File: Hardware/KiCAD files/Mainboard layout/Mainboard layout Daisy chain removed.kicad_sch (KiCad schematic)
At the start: 90 parts, among them J10 Conn_01x02, J11 Conn_01x04, J12 JST_06, J13 Conn_01x08, J14 Conn_01x08, J15 Screw_Terminal_2_P5.00mm, J17 PINHD_1x8_Male, J18 PINHD_1x8_Male, J19 PINHD_1x8_Male, J2 Screw_Terminal_2_P5.00mm, J20 PINHD_1x8_Male, J22 PINHD_1x8_Male, J23 PINHD_1x8_Male, J24 PINHD_1x8_Male, J25 Conn_01x04, J26 Conn_01x04, J27 Conn_01x04, J28 PINHD_1x8_Male, J3 Screw_Terminal_2_P3.50mm, J30 USB-A1VSB6, J31 JST_03, J32 USB-A1VSB6, J34 JST_03, J35 JST_03, J36 JST_03, J37 JST_03, J38 JST_03, J4 JST_06, J5 Conn_01x04, J6 JST_06, J7 JST_06, J8 Conn_01x06, J9 Conn_01x10, Q1 BS170, Q2 2DD1664, SW1 210-4MS, SW2 210-4MS, SW3 210-4MS, SW4 210-4MS, SW8 Push_Button, SW9 Push_Button, U1 CP2102-GM, U12 ESP32-S3-WROOM-1, U2 PCA9534PW_118, U4 PCA9534PW_118

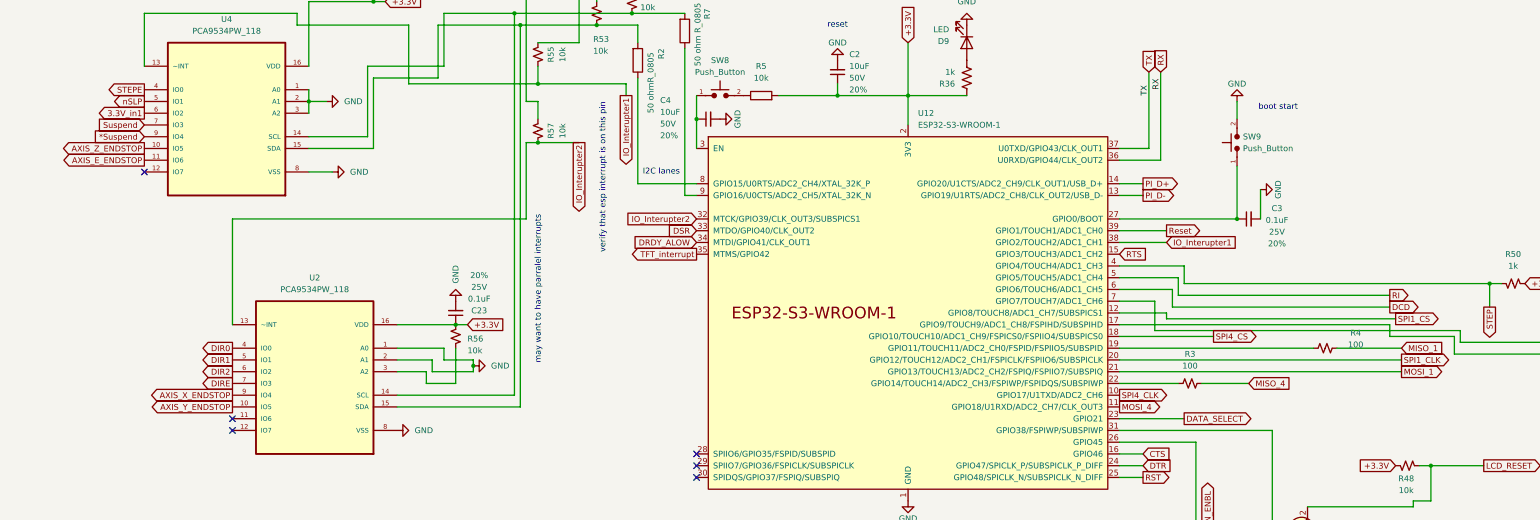
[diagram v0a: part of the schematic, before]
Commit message: part of the way through next iteration
Non-daisy chain Mainboard is ~50% through
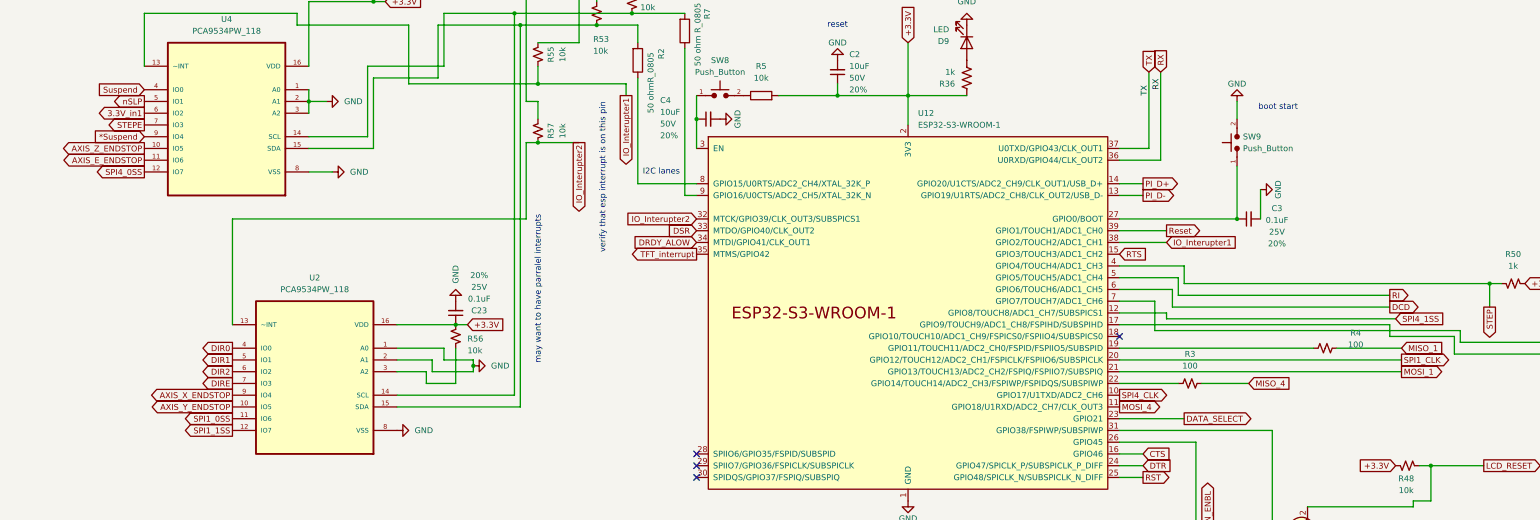
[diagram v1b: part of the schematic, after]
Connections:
- net SPI1_CS: no longer U12.12 (GPIO8/TOUCH8/ADC1_CH7/SUBSPICS1)
- net SPI4_CS: no longer U12.18 (GPIO10/TOUCH10/ADC1_CH9/FSPICS0/FSPIIO4/SUBSPICS0)
- net STEPE: now also U4.7 (IO3); no longer U4.4 (IO0)
- net Suspend: now also U4.4 (IO0); no longer U4.7 (IO3)
- net SPI4_0SS: now reaches U4.12 (IO7)
- net SPI1_0SS: now reaches U2.11 (IO6)
- net SPI1_1SS: now reaches U2.12 (IO7)
- new net SPI4_1SS: U12.12 (GPIO8/TOUCH8/ADC1_CH7/SUBSPICS1)
- no-connect marks 34 -> 32
